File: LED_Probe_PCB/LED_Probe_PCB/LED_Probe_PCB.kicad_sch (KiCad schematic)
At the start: 9 parts, among them J5 Conn_01x40

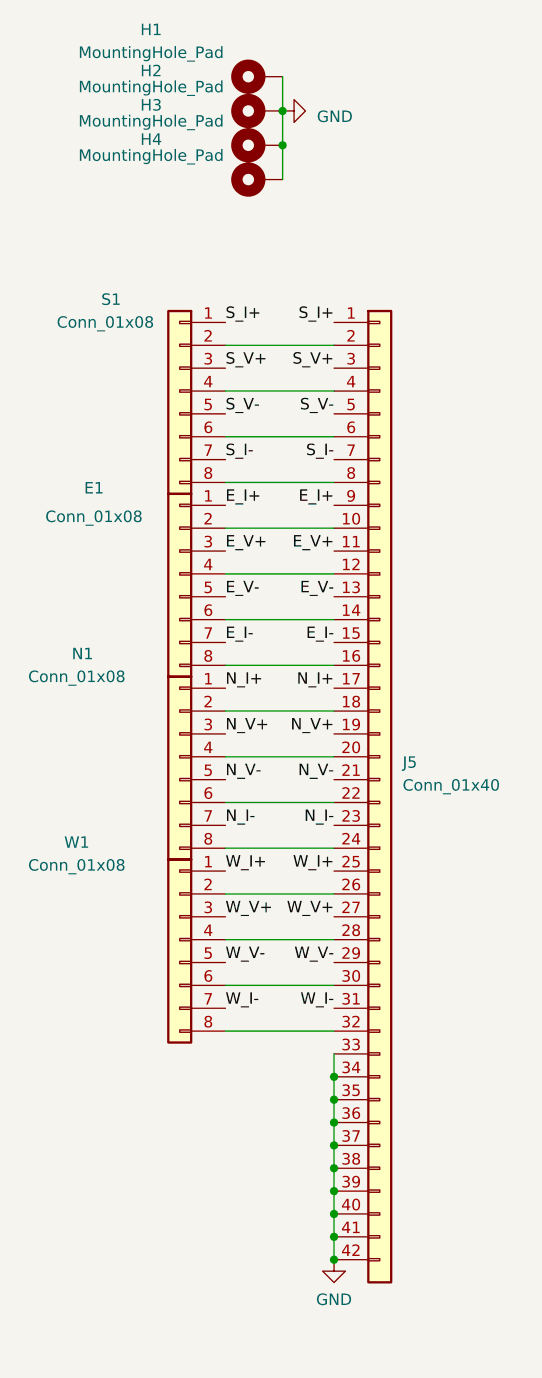
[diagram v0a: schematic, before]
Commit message: update to 2x 20P
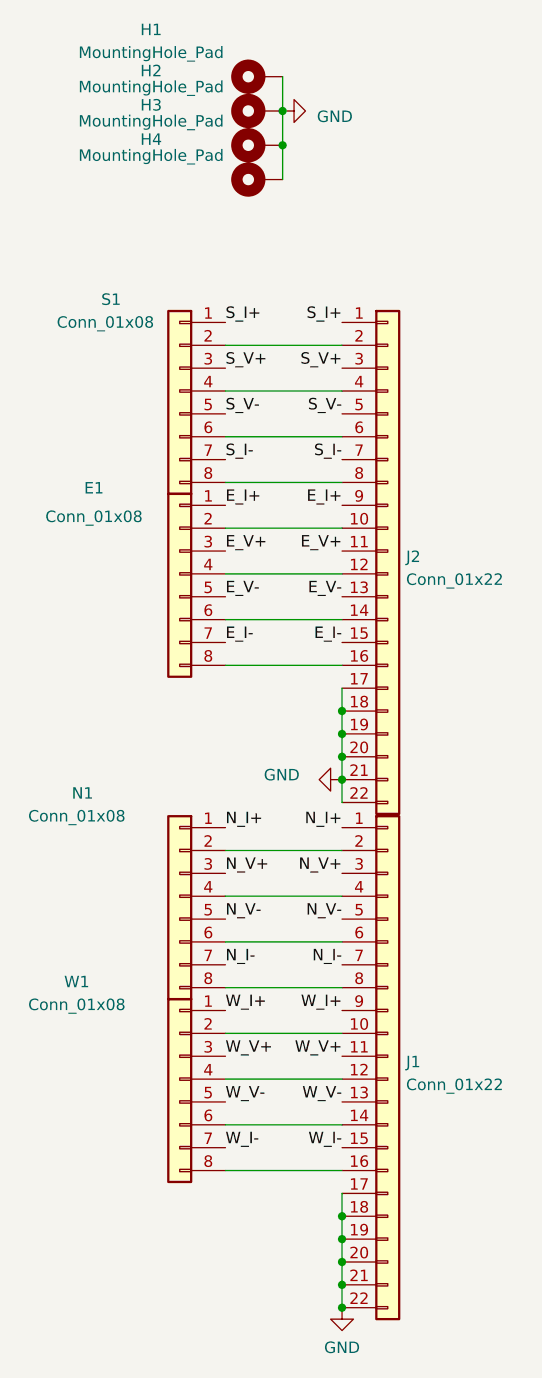
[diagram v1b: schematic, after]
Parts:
- removed J5: Conn_01x40, 0_led_probe_footprint_lib:FPC-SMD_P0.50-40P_FGS-XJ-H2.0, symbol Connector_Generic:Conn_01x40
- added J1, J2: Conn_01x22, 0_led_probe_footprint_lib:FPC-SMD_20P-P0.50_XUNPU_FPC-05F-20PH20, symbol Connector_Generic:Conn_01x22
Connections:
- net E_I+: now also J2.9 (Pin_9)
- net E_I-: now also J2.15 (Pin_15)
- net E_V+: now also J2.11 (Pin_11)
- net E_V-: now also J2.13 (Pin_13)
- net GND: now also J1.17 (Pin_17), J1.18 (Pin_18), J1.19 (Pin_19), J1.20 (Pin_20), J1.21 (Pin_21), J1.22 (Pin_22), J2.17 (Pin_17), J2.18 (Pin_18), J2.19 (Pin_19), J2.20 (Pin_20), J2.21 (Pin_21), J2.22 (Pin_22)
- net N_I+: now also J1.1 (Pin_1)
- net N_I-: now also J1.7 (Pin_7)
- net N_V+: now also J1.3 (Pin_3)
- net N_V-: now also J1.5 (Pin_5)
- net S_I+: now also J2.1 (Pin_1)
- net S_I-: now also J2.7 (Pin_7)
- net S_V+: now also J2.3 (Pin_3)
- net S_V-: now also J2.5 (Pin_5)
- net W_I+: now also J1.9 (Pin_9)
- net W_I-: now also J1.15 (Pin_15)
- net W_V+: now also J1.11 (Pin_11)
- net W_V-: now also J1.13 (Pin_13)
- net at S1.2 (Pin_2): now also J2.2 (Pin_2)
- net at S1.4 (Pin_4): now also J2.4 (Pin_4)
- net at S1.6 (Pin_6): now also J2.6 (Pin_6)
- net at S1.8 (Pin_8): now also J2.8 (Pin_8)
- net at E1.2 (Pin_2): now also J2.10 (Pin_10)
- net at E1.4 (Pin_4): now also J2.12 (Pin_12)
- net at E1.6 (Pin_6): now also J2.14 (Pin_14)
- net at E1.8 (Pin_8): now also J2.16 (Pin_16)
- net at N1.2 (Pin_2): now also J1.2 (Pin_2)
- net at N1.4 (Pin_4): now also J1.4 (Pin_4)
- net at N1.6 (Pin_6): now also J1.6 (Pin_6)
- net at N1.8 (Pin_8): now also J1.8 (Pin_8)
- net at W1.2 (Pin_2): now also J1.10 (Pin_10)
- net at W1.4 (Pin_4): now also J1.12 (Pin_12)
- net at W1.6 (Pin_6): now also J1.14 (Pin_14)
- net at W1.8 (Pin_8): now also J1.16 (Pin_16)
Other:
- moved on the sheet: N1, W1
